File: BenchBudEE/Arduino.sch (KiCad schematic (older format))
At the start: 0 parts

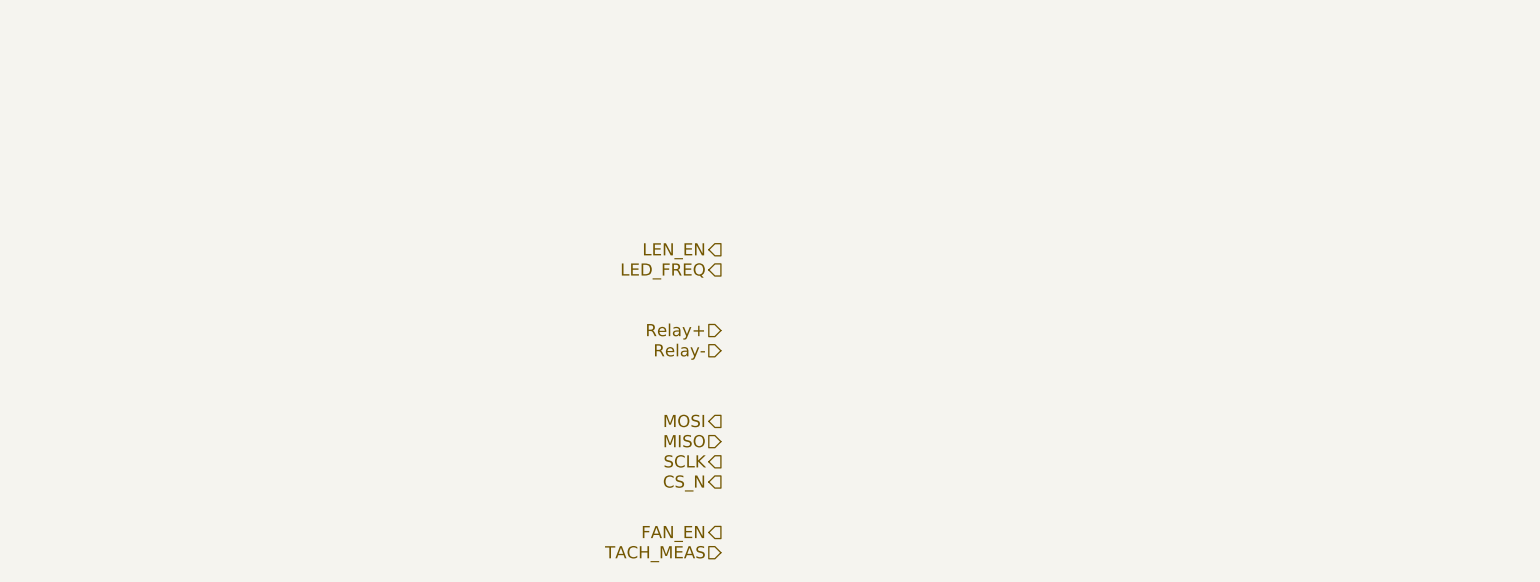
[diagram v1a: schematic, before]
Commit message: Completing schematics from week 3 videos.
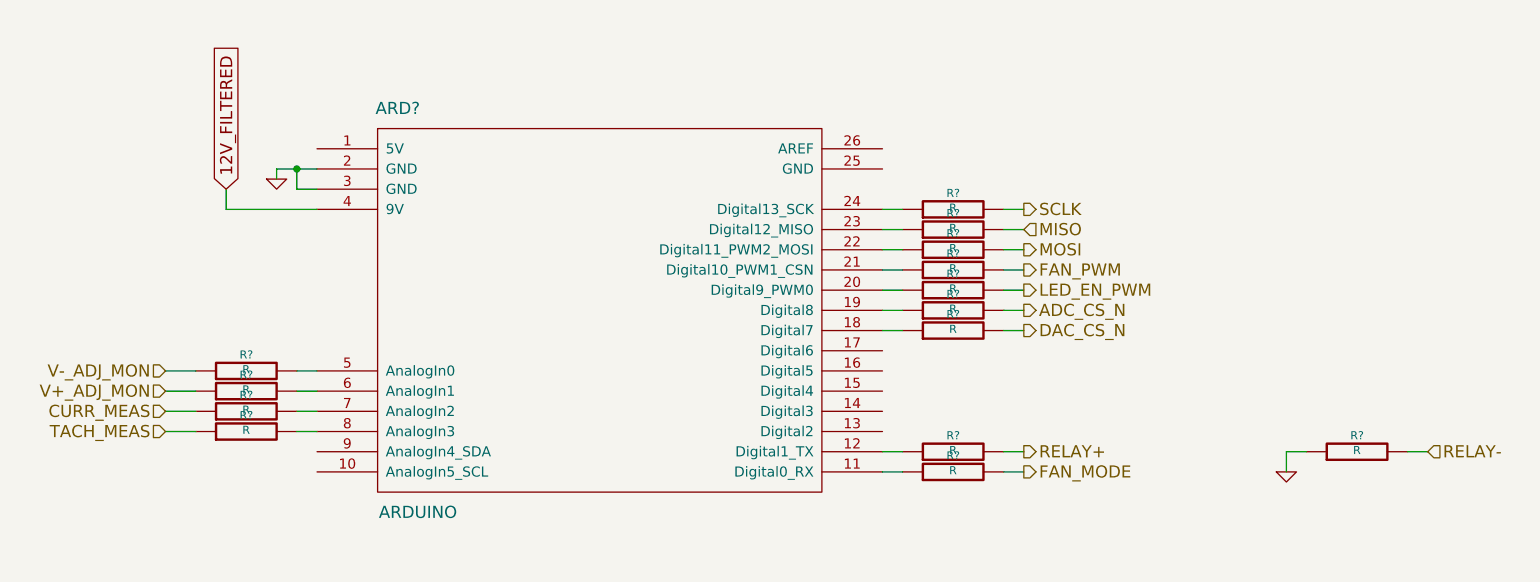
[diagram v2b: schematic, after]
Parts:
- added ARD?: ARDUINO, ~, symbol ARDUINO
- added R? (x14): R, ~, symbol R
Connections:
- net MISO: now also R?.2
- net MOSI: now also R?.2
- net SCLK: now also R?.2
- net TACH_MEAS: now also R?.1
- new net: ARD?.11 (Digital0_RX), R?.1
- new net: ARD?.12 (Digital1_TX), R?.1
- new net: ARD?.18 (Digital7), R?.1
- new net: ARD?.19 (Digital8), R?.1
- new net: ARD?.20 (Digital9_PWM0), R?.1
- new net: ARD?.21 (Digital10_PWM1_CSN), R?.1
- new net: ARD?.22 (Digital11_PWM2_MOSI), R?.1
- new net: ARD?.23 (Digital12_MISO), R?.1
- new net: ARD?.24 (Digital13_SCK), R?.1
- new net: ARD?.5 (AnalogIn0), R?.2
- new net: ARD?.6 (AnalogIn1), R?.2
- new net: ARD?.7 (AnalogIn2), R?.2
- new net: ARD?.8 (AnalogIn3), R?.2
- new net 12V_FILTERED: ARD?.4 (9V)
- new net ADC_CS_N: R?.2
- new net CURR_MEAS: R?.1
- new net DAC_CS_N: R?.2
- new net FAN_MODE: R?.2
- new net FAN_PWM: R?.2
- new net GND: ARD?.2 (GND), ARD?.3 (GND), R?.1
- new net LED_EN_PWM: R?.2
- new net RELAY+: R?.2
- new net RELAY-: R?.2
- new net V+_ADJ_MON: R?.1
- new net V-_ADJ_MON: R?.1

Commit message: checking in all my local changes before syncing to chris's repo.
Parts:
- gave numbers to parts that had none: 15
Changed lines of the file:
@@
 Sheet 9 9
 Title ""
-Date "24 feb 2014"
+Date "2 mar 2014"
 Rev ""
 Comp ""
@@
 TACH_MEAS
 $Comp
-L ARDUINO ARD?
+L ARDUINO ARD1
 U 1 1 530DDB6E
 P 5300 3200
-F 0 "ARD?" H 4300 4350 60  0000 C CNN
+F 0 "ARD1" H 4300 4350 60  0000 C CNN
 F 1 "ARDUINO" H 4400 2350 60  0000 C CNN
 F 2 "~" H 5650 3200 60  0000 C CNN
@@
 V-_ADJ_MON
 $Comp
-L R R?
+L R R31
 U 1 1 530E0AA2
 P 3550 3350
-F 0 "R?" V 3630 3350 40  0000 C CNN
+F 0 "R31" V 3630 3350 40  0000 C CNN
 F 1 "R" V 3557 3351 40  0000 C CNN
 F 2 "~" V 3480 3350 30  0000 C CNN
@@
 $EndComp
 $Comp
-L R R?
+L R R32
 U 1 1 530E0AB1
 P 3550 3450
-F 0 "R?" V 3630 3450 40  0000 C CNN
+F 0 "R32" V 3630 3450 40  0000 C CNN
 F 1 "R" V 3557 3451 40  0000 C CNN
 F 2 "~" V 3480 3450 30  0000 C CNN
@@
 $EndComp
 $Comp
-L R R?
+L R R33
 U 1 1 530E0AC0
 P 3550 3550
-F 0 "R?" V 3630 3550 40  0000 C CNN
+F 0 "R33" V 3630 3550 40  0000 C CNN
 F 1 "R" V 3557 3551 40  0000 C CNN
 F 2 "~" V 3480 3550 30  0000 C CNN
@@
 $EndComp
 $Comp
-L R R?
+L R R34
 U 1 1 530E0ACF
 P 3550 3650
-F 0 "R?" V 3630 3650 40  0000 C CNN
+F 0 "R34" V 3630 3650 40  0000 C CNN
 F 1 "R" V 3557 3651 40  0000 C CNN
 F 2 "~" V 3480 3650 30  0000 C CNN
@@
 	3900 3650 3800 3650
 $Comp
-L R R?
+L R R35
 U 1 1 530E0B10
 P 7050 2550
-F 0 "R?" V 7130 2550 40  0000 C CNN
+F 0 "R35" V 7130 2550 40  0000 C CNN
 F 1 "R" V 7057 2551 40  0000 C CNN
 F 2 "~" V 6980 2550 30  0000 C CNN
@@
 $EndComp
 $Comp
-L R R?
+L R R36
 U 1 1 530E0B1F
 P 7050 2650
-F 0 "R?" V 7130 2650 40  0000 C CNN
+F 0 "R36" V 7130 2650 40  0000 C CNN
 F 1 "R" V 7057 2651 40  0000 C CNN
 F 2 "~" V 6980 2650 30  0000 C CNN
@@
 $EndComp
 $Comp
-L R R?
+L R R37
 U 1 1 530E0B2E
 P 7050 2750
-F 0 "R?" V 7130 2750 40  0000 C CNN
+F 0 "R37" V 7130 2750 40  0000 C CNN
 F 1 "R" V 7057 2751 40  0000 C CNN
 F 2 "~" V 6980 2750 30  0000 C CNN
@@
 $EndComp
 $Comp
-L R R?
+L R R38
 U 1 1 530E0B3D
 P 7050 2850
-F 0 "R?" V 7130 2850 40  0000 C CNN
+F 0 "R38" V 7130 2850 40  0000 C CNN
 F 1 "R" V 7057 2851 40  0000 C CNN
 F 2 "~" V 6980 2850 30  0000 C CNN
@@
 	7300 2850 7400 2850
 $Comp
-L R R?
+L R R39
 U 1 1 530E0BD4
 P 7050 2950
-F 0 "R?" V 7130 2950 40  0000 C CNN
+F 0 "R39" V 7130 2950 40  0000 C CNN
 F 1 "R" V 7057 2951 40  0000 C CNN
 F 2 "~" V 6980 2950 30  0000 C CNN
@@
 DAC_CS_N
 $Comp
-L R R?
+L R R40
 U 1 1 530E0BFE
 P 7050 3050
-F 0 "R?" V 7130 3050 40  0000 C CNN
+F 0 "R40" V 7130 3050 40  0000 C CNN
 F 1 "R" V 7057 3051 40  0000 C CNN
 F 2 "~" V 6980 3050 30  0000 C CNN
@@
 $EndComp
 $Comp
-L R R?
+L R R41
 U 1 1 530E0C04
 P 7050 3150
-F 0 "R?" V 7130 3150 40  0000 C CNN
+F 0 "R41" V 7130 3150 40  0000 C CNN
 F 1 "R" V 7057 3151 40  0000 C CNN
 F 2 "~" V 6980 3150 30  0000 C CNN
@@
 	7300 3150 7400 3150
 $Comp
-L R R?
+L R R43
 U 1 1 530E0C5C
 P 7050 3850
-F 0 "R?" V 7130 3850 40  0000 C CNN
+F 0 "R43" V 7130 3850 40  0000 C CNN
 F 1 "R" V 7057 3851 40  0000 C CNN
 F 2 "~" V 6980 3850 30  0000 C CNN
@@
 	6700 3850 6800 3850
 $Comp
-L R R?
+L R R42
 U 1 1 530E0C91
 P 7050 3750
-F 0 "R?" V 7130 3750 40  0000 C CNN
+F 0 "R42" V 7130 3750 40  0000 C CNN
 F 1 "R" V 7057 3751 40  0000 C CNN
 F 2 "~" V 6980 3750 30  0000 C CNN
@@
 RELAY-
 $Comp
-L R R?
+L R R44
 U 1 1 530E0CCA
 P 9050 3750
-F 0 "R?" V 9130 3750 40  0000 C CNN
+F 0 "R44" V 9130 3750 40  0000 C CNN
 F 1 "R" V 9057 3751 40  0000 C CNN
 F 2 "~" V 8980 3750 30  0000 C CNN
@@
 $EndComp
 $Comp
-L GND #PWR?
+L GND #PWR43
 U 1 1 530E0CD2
 P 8700 3850
-F 0 "#PWR?" H 8700 3850 30  0001 C CNN
+F 0 "#PWR43" H 8700 3850 30  0001 C CNN
 F 1 "GND" H 8700 3780 30  0001 C CNN
 F 2 "" H 8700 3850 60  0000 C CNN
@@
 	9300 3750 9400 3750
 $Comp
-L GND #PWR?
+L GND #PWR42
 U 1 1 530E0D19
 P 3700 2400
-F 0 "#PWR?" H 3700 2400 30  0001 C CNN
+F 0 "#PWR42" H 3700 2400 30  0001 C CNN
 F 1 "GND" H 3700 2330 30  0001 C CNN
 F 2 "" H 3700 2400 60  0000 C CNN
